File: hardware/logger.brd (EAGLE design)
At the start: 33.5 x 32.9 mm, 40 parts, among them J1 MICRO_USB_B_HIROSE_ZX62-B-5PA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, SW1 TVAF06-A020B-R, U2 NJM12888F, X1 FA-238

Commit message: loggerの基盤終わりました！
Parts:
- moved C15 6.60 mm to (-5.21, -2.54), turned to 180 degrees
- moved C16 2.84 mm to (8.89, 8.89), turned to 90 degrees
- moved C10 2.16 mm to (2.16, -2.41)
- moved C9 2.16 mm to (5.21, -2.41)
- moved C11 1.15 mm to (-3.68, -3.94)
- moved C14 1.15 mm to (-6.73, -3.94)
- moved C6 0.92 mm to (1.27, -3.56)
- moved C18 0.64 mm to (-8.26, -2.54), turned to 180 degrees
- moved C17 0.13 mm to (-11.3, -2.54)
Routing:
- net GND: track 112.9 -> 223.9 mm, vias 71 -> 69
- net N$1: track 0.00 -> 27.8 mm, vias 0 -> 3
- net VDD: track 73.0 -> 97.9 mm, vias 6 -> 11
- net I2C0_SDA: track 0.00 -> 21.9 mm, vias 0 -> 2
- net SPI0_MISO: track 0.00 -> 15.4 mm, vias 0 -> 2
- net I2C0_SCL: track 0.00 -> 15.4 mm, vias 0 -> 2
- net SPI1_MISO: track 0.00 -> 15.4 mm, vias 0 -> 2
- net SPI1_CS: track 0.00 -> 14.6 mm, vias 0 -> 2
- net SPI0_CS: track 0.00 -> 8.79 mm, vias 0 -> 2
- net SPI1_MOSI: track 0.00 -> 8.54 mm, vias 0 -> 2
- net SPI0_MOSI: track 0.00 -> 7.19 mm, vias 0 -> 2
- net SPI1_SCK: track 0.00 -> 7.18 mm, vias 0 -> 2
- net SPI0_SCK: track 0.00 -> 7.00 mm, vias 0 -> 2
- net LED1: track 21.8 -> 17.7 mm, vias 2 -> 4
- net TX1: track 19.8 -> 21.4 mm
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
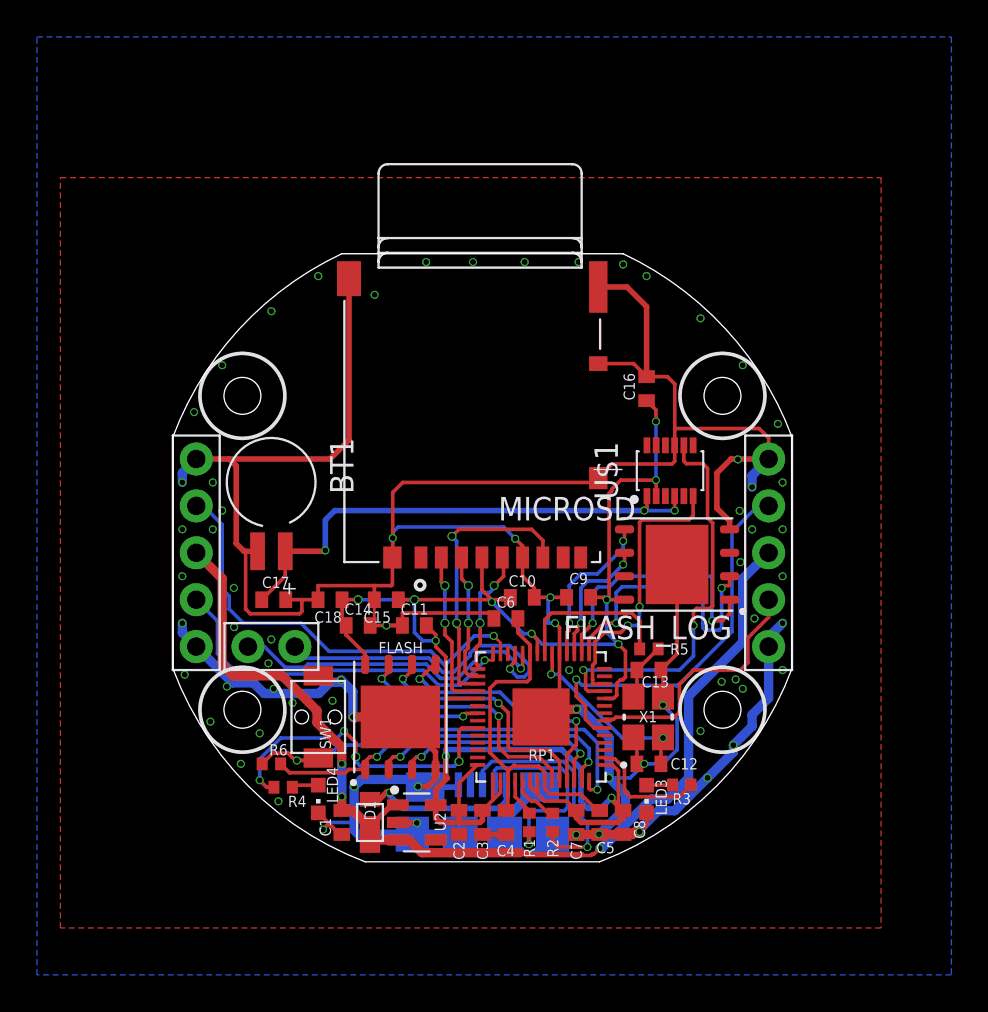
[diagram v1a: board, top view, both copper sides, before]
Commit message: べたGND前です。esp32のschはノータッチなのでここに上がってないです。よろしくお願いします。
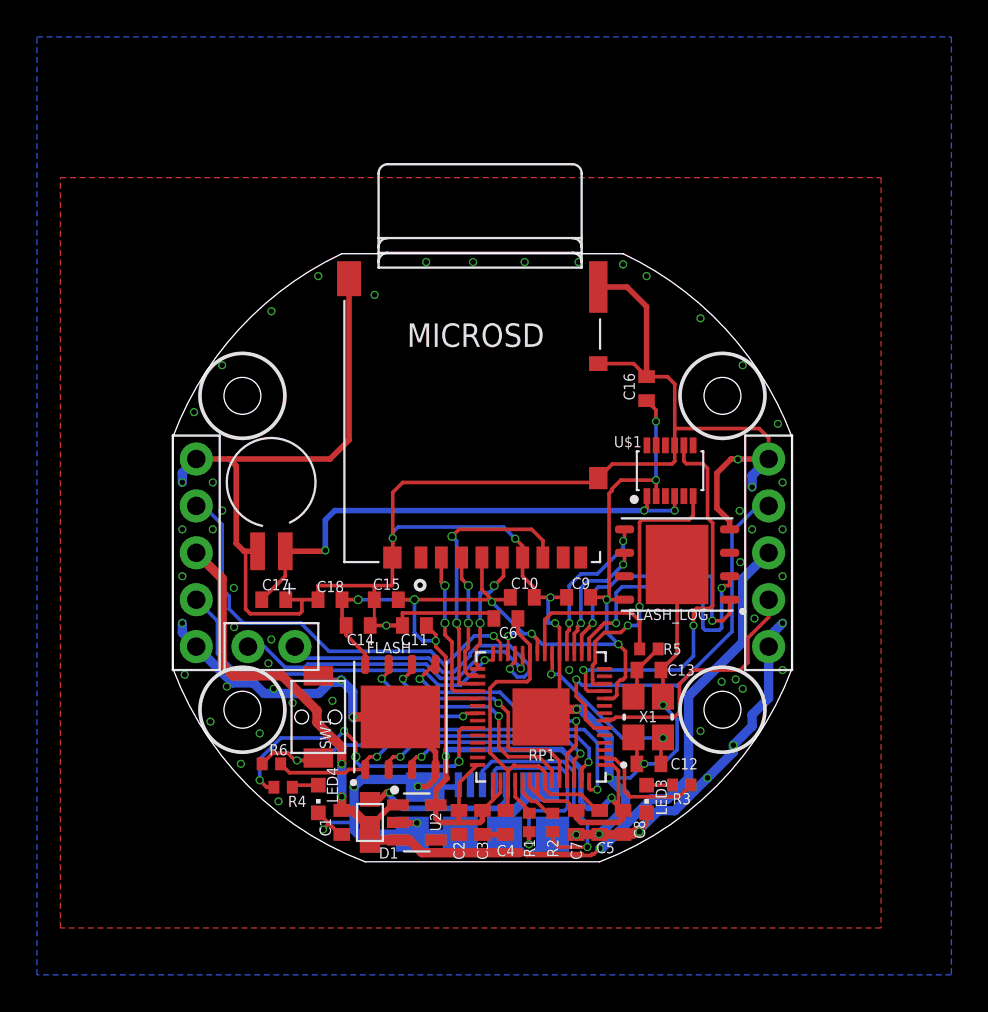
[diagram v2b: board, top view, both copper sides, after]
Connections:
- net VDD: now also RP1.26
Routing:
- net VDD: track 97.9 -> 100.0 mm, vias 11 -> 12

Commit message: LiPoのだけできなかったのですが、それ以外のべたGND済のものです。
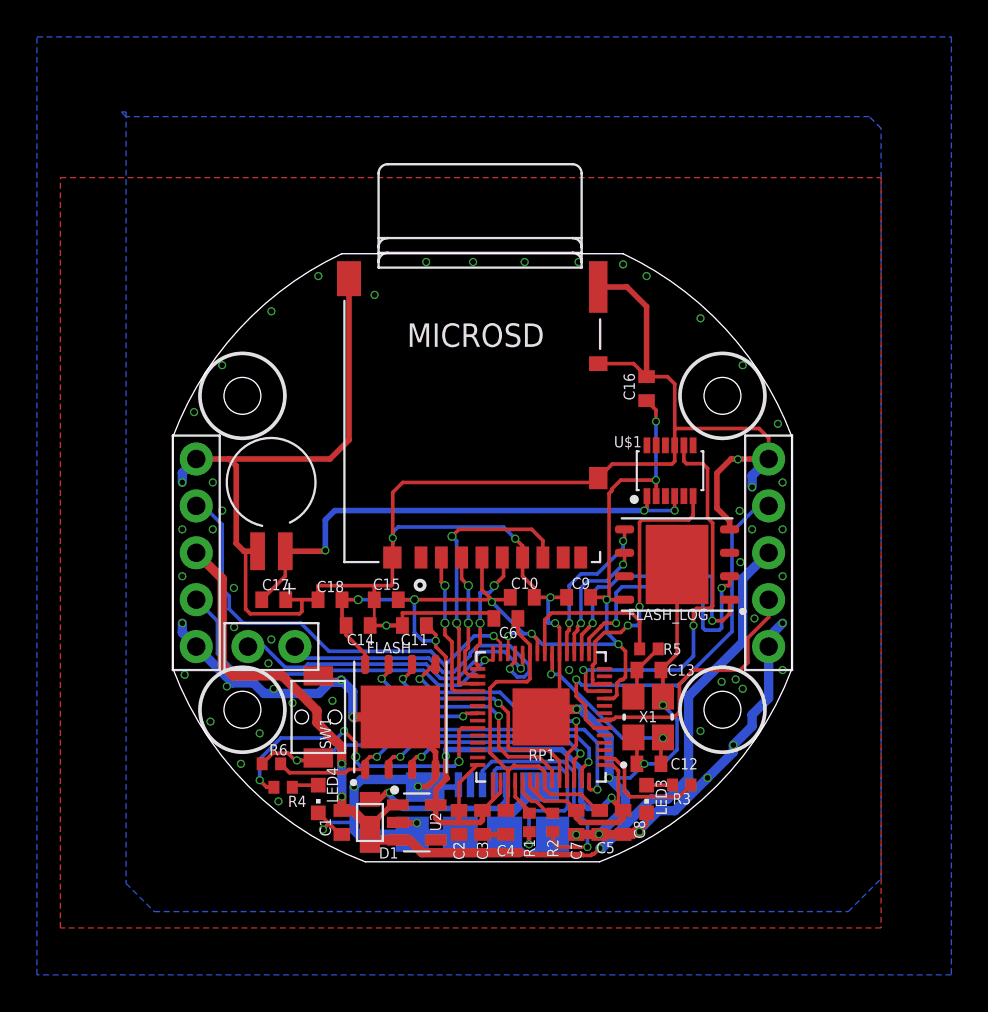
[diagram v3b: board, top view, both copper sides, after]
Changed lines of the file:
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@@
 <wire x1="-4.318" y1="3.81" x2="-4.8585" y2="3.2695" width="0.2" layer="1"/>
 <wire x1="-4.8585" y1="3.2695" x2="-4.8585" y2="0.7965" width="0.2" layer="1"/>
+<polygon width="0.1524" layer="16">
+<vertex x="-19.304" y="23.876"/>
+<vertex x="-19.304" y="-17.907"/>
+<vertex x="-17.78" y="-19.431"/>
+<vertex x="19.812" y="-19.431"/>
+<vertex x="21.59" y="-17.653"/>
+<vertex x="21.59" y="22.987"/>
+<vertex x="20.955" y="23.622"/>
+<vertex x="-19.304" y="23.622"/>
+<vertex x="-19.558" y="23.876"/>
+</polygon>
 <wire x1="11.811" y1="12.7" x2="14.097" y2="10.16" width="0" layer="19" extent="1-1"/>
 <wire x1="16.002" y1="6.985" x2="14.097" y2="10.16" width="0" layer="19" extent="1-1"/>

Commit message: 微修正
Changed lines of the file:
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@@
 <via x="14.605" y="3.556" extent="1-16" drill="0.3"/>
 <via x="14.605" y="1.27" extent="1-16" drill="0.3"/>
-<via x="13.97" y="-0.508" extent="1-16" drill="0.3"/>
+<via x="13.97" y="-0.5395" extent="1-16" drill="0.3"/>
 <via x="14.732" y="-3.556" extent="1-16" drill="0.3"/>
 <via x="13.716" y="-6.858" extent="1-16" drill="0.3"/>
@@
 <wire x1="-9.906" y1="-3.302" x2="-9.779" y2="-3.175" width="0.2" layer="1"/>
 <wire x1="-9.779" y1="-3.175" x2="-9.779" y2="-2.54" width="0.2" layer="1"/>
-<wire x1="-4.8585" y1="0.7965" x2="-4.8585" y2="0.508" width="0.2" layer="1"/>
-<wire x1="-4.8585" y1="0.508" x2="-4.8585" y2="-0.3625" width="0.2" layer="1"/>
+<wire x1="-4.8585" y1="0.7965" x2="-4.8585" y2="-0.3625" width="0.2" layer="1"/>
 <wire x1="-4.8585" y1="-0.3625" x2="-4.877" y2="-0.381" width="0.2" layer="1"/>
 <wire x1="1.778" y1="0.762" x2="2.173" y2="0.367" width="0.2" layer="1"/>
@@
 <vertex x="21.59" y="22.987"/>
 <vertex x="20.955" y="23.622"/>
-<vertex x="-19.304" y="23.622"/>
-<vertex x="-19.558" y="23.876"/>
+<vertex x="-19.05" y="23.622"/>
 </polygon>
-<wire x1="11.811" y1="12.7" x2="14.097" y2="10.16" width="0" layer="19" extent="1-1"/>
-<wire x1="16.002" y1="6.985" x2="14.097" y2="10.16" width="0" layer="19" extent="1-1"/>
-<wire x1="15.5" y1="5.08" x2="16.002" y2="6.985" width="0" layer="19" extent="1-1"/>
-<wire x1="6.35" y1="-15.255" x2="6.3165" y2="-15.241" width="0" layer="19" extent="1-1"/>
-<wire x1="-1.27" y1="-15.255" x2="-1.2" y2="-15.24" width="0" layer="19" extent="1-16"/>
-<wire x1="1.27" y1="-15.255" x2="1.2" y2="-15.24" width="0" layer="19" extent="1-16"/>
-<wire x1="-3.49" y1="-12.6605" x2="-3.1" y2="-12.69" width="0" layer="19" extent="16-16"/>
-<wire x1="-8.124" y1="-8.0145" x2="-7.678" y2="-6.9595" width="0" layer="19" extent="16-16"/>
-<wire x1="13.933" y1="2.273" x2="13.386" y2="1.27" width="0" layer="19" extent="1-1"/>
-<wire x1="14.605" y1="1.27" x2="13.386" y2="1.27" width="0" layer="19" extent="1-1"/>
-<wire x1="16.256" y1="3.81" x2="15.5" y2="5.08" width="0" layer="19" extent="1-1"/>
-<wire x1="16.256" y1="-6.35" x2="15.5" y2="-5.08" width="0" layer="19" extent="1-1"/>
-<wire x1="14.732" y1="-3.556" x2="16.256" y2="-3.81" width="0" layer="19" extent="1-1"/>
-<wire x1="-14.605" y1="3.81" x2="-15.5" y2="5.08" width="0" layer="19" extent="1-1"/>
-<wire x1="-14.097" y1="2.286" x2="-14.605" y2="3.81" width="0" layer="19" extent="1-1"/>
-<wire x1="-14.605" y1="1.27" x2="-14.097" y2="2.286" width="0" layer="19" extent="1-1"/>
-<wire x1="-16.129" y1="-6.604" x2="-15.5" y2="-5.08" width="0" layer="19" extent="1-1"/>
-<wire x1="-16.256" y1="1.27" x2="-14.605" y2="1.27" width="0" layer="19" extent="1-1"/>
-<wire x1="16.256" y1="1.27" x2="14.605" y2="1.27" width="0" layer="19" extent="1-1"/>
-<wire x1="13.8385" y1="5.0585" x2="15.5" y2="5.08" width="0" layer="19" extent="1-1"/>
-<wire x1="-5.842" y1="13.97" x2="-7.227" y2="14.846" width="0" layer="19" extent="1-1"/>
-<wire x1="-8.89" y1="14.986" x2="-7.227" y2="14.846" width="0" layer="19" extent="1-1"/>
-<wire x1="5.207" y1="15.748" x2="6.273" y2="14.396" width="0" layer="19" extent="1-1"/>
-<wire x1="7.62" y1="15.621" x2="6.273" y2="14.396" width="0" layer="19" extent="1-1"/>
-<wire x1="8.89" y1="14.986" x2="7.62" y2="15.621" width="0" layer="19" extent="1-1"/>
-<wire x1="13.97" y1="-0.508" x2="13.386" y2="1.27" width="0" layer="19" extent="1-1"/>
-<wire x1="11.811" y1="-9.652" x2="13.589" y2="-10.414" width="0" layer="19" extent="1-1"/>
-<wire x1="-10.287" y1="-8.128" x2="-8.89" y2="-6.665" width="0" layer="19" extent="1-1"/>
-<wire x1="-11.303" y1="-7.366" x2="-10.287" y2="-8.128" width="0" layer="19" extent="1-1"/>
-<wire x1="-11.592" y1="-5.985" x2="-11.303" y2="-7.366" width="0" layer="19" extent="1-1"/>
-<wire x1="-11.4345" y1="-4.6935" x2="-11.592" y2="-5.985" width="0" layer="19" extent="1-1"/>
-<wire x1="-13.45" y1="-4.0235" x2="-11.4345" y2="-4.6935" width="0" layer="19" extent="1-1"/>
-<wire x1="-13.462" y1="-1.905" x2="-13.45" y2="-4.0235" width="0" layer="19" extent="1-1"/>
-<wire x1="-11.049" y1="-13.462" x2="-8.89" y2="-14.085" width="0" layer="19" extent="1-1"/>
-<wire x1="-13.843" y1="-7.239" x2="-16.129" y2="-6.604" width="0" layer="19" extent="1-1"/>
-<wire x1="-14.732" y1="-9.144" x2="-13.843" y2="-7.239" width="0" layer="19" extent="1-1"/>
-<wire x1="14.097" y1="-7.366" x2="16.256" y2="-6.35" width="0" layer="19" extent="1-1"/>
-<wire x1="13.716" y1="-6.858" x2="14.097" y2="-7.366" width="0" layer="19" extent="1-1"/>
-<wire x1="12.954" y1="-6.985" x2="13.716" y2="-6.858" width="0" layer="19" extent="1-1"/>
-<wire x1="-12.065" y1="-9.779" x2="-10.287" y2="-8.128" width="0" layer="19" extent="1-1"/>
-<wire x1="-13.081" y1="-11.43" x2="-12.065" y2="-9.779" width="0" layer="19" extent="1-1"/>
-<wire x1="16.256" y1="-1.27" x2="13.97" y2="-0.508" width="0" layer="19" extent="1-1"/>
-<wire x1="-16.256" y1="-1.27" x2="-16.256" y2="-3.81" width="0" layer="19" extent="1-1"/>
-<wire x1="-15.621" y1="7.62" x2="-15.5" y2="5.08" width="0" layer="19" extent="1-1"/>
-<wire x1="2.286" y1="15.748" x2="5.207" y2="15.748" width="0" layer="19" extent="1-1"/>
-<wire x1="-0.508" y1="15.748" x2="2.286" y2="15.748" width="0" layer="19" extent="1-1"/>
-<wire x1="-3.048" y1="15.748" x2="-0.508" y2="15.748" width="0" layer="19" extent="1-1"/>
-<wire x1="-14.097" y1="10.16" x2="-15.621" y2="7.62" width="0" layer="19" extent="1-1"/>
-<wire x1="-11.43" y1="13.081" x2="-8.89" y2="14.986" width="0" layer="19" extent="1-1"/>
 </signal>
 <signal name="USB_DM">
